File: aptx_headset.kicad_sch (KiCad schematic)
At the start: 63 parts, among them J1 AudioJack4, J2 Conn_01x03, SW1 vol+, SW2 vol-, SW3 next, SW4 prev, SW5 pp/call, SW6 mute, U1 OPA1664, U2 CSR8645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

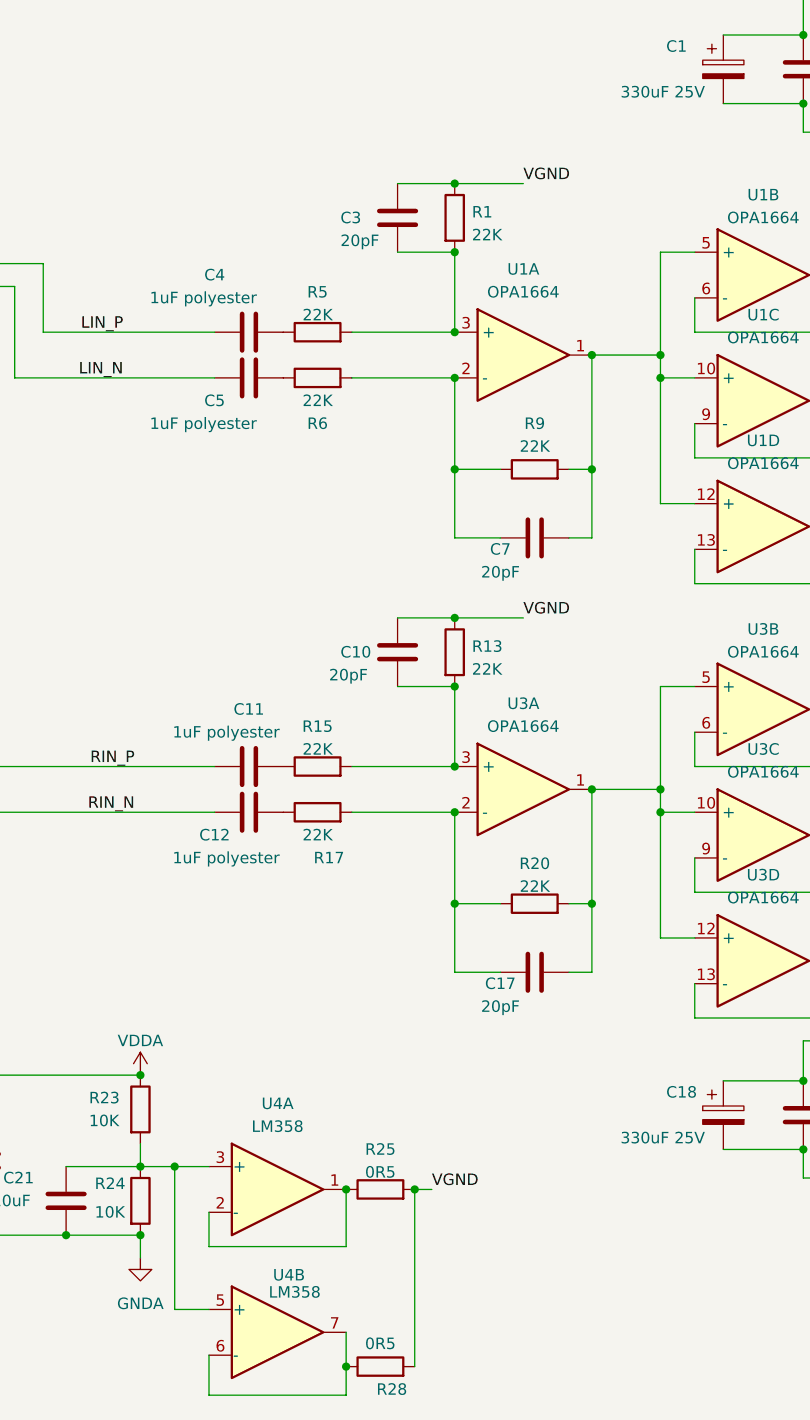
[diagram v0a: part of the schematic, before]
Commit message: separate buffered VGND
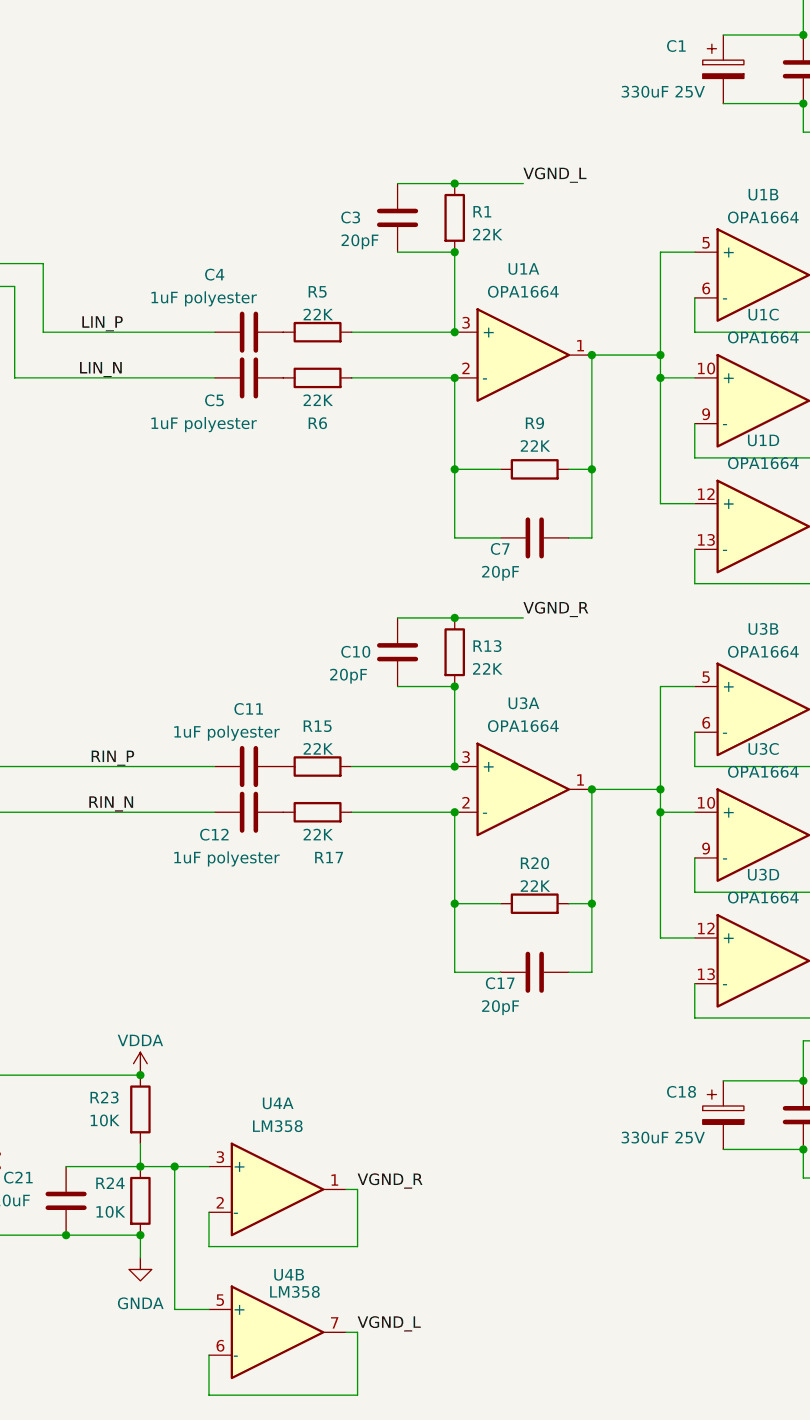
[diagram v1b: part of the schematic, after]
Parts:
- removed R25, R28: 0R5, 00_hari:R_0603_1608Metric_Pad0.98x0.95mm_HandSolder, symbol Device:R
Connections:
- net VGND_R: now reaches U4.1, U4.2 (-)
- net VGND_R: now also C10.1, R13.1
- net VGND_L: now reaches U4.6 (-), U4.7
- net VGND_L: now also C3.1, R1.1
- removed net VGND: C10.1, C3.1, R1.1, R13.1
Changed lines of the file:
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@@
   (junction (at 27.305 57.785) (diameter 0) (color 0 0 0 0)
   )
-  (junction (at 163.83 180.34) (diameter 0) (color 0 0 0 0)
-  )
   (junction (at 73.025 127.635) (diameter 0) (color 0 0 0 0)
   )
@@
   (junction (at 217.805 135.255) (diameter 0) (color 0 0 0 0)
   )
-  (junction (at 171.45 160.655) (diameter 0) (color 0 0 0 0)
-  )
   (junction (at 175.895 97.155) (diameter 0) (color 0 0 0 0)
   )
@@
   )
   (junction (at 132.715 165.735) (diameter 0) (color 0 0 0 0)
-  )
-  (junction (at 163.83 160.655) (diameter 0) (color 0 0 0 0)
   )
   (junction (at 217.805 107.315) (diameter 0) (color 0 0 0 0)
@@
     (stroke (width 0) (type default))
   )
-  (wire (pts (xy 148.59 183.515) (xy 163.83 183.515))
+  (wire (pts (xy 148.59 183.515) (xy 165.1 183.515))
     (stroke (width 0) (type default))
   )
@@
     (stroke (width 0) (type default))
   )
-  (wire (pts (xy 148.59 167.005) (xy 163.83 167.005))
+  (wire (pts (xy 148.59 167.005) (xy 165.1 167.005))
     (stroke (width 0) (type default))
   )
@@
     (stroke (width 0) (type default))
   )
-  (wire (pts (xy 163.83 176.53) (xy 163.83 180.34))
-    (stroke (width 0) (type default))
-  )
   (wire (pts (xy 202.565 61.595) (xy 202.565 65.405))
     (stroke (width 0) (type default))
@@
     (stroke (width 0) (type default))
   )
-  (wire (pts (xy 171.45 160.655) (xy 171.45 180.34))
-    (stroke (width 0) (type default))
-  )
   (wire (pts (xy 132.715 165.735) (xy 140.97 165.735))
     (stroke (width 0) (type default))
@@
     (stroke (width 0) (type default))
   )
-  (wire (pts (xy 163.83 160.655) (xy 163.83 167.005))
+  (wire (pts (xy 165.1 160.655) (xy 165.1 167.005))
     (stroke (width 0) (type default))
   )
@@
     (stroke (width 0) (type default))
   )
-  (wire (pts (xy 173.355 160.655) (xy 171.45 160.655))
-    (stroke (width 0) (type default))
-  )
   (wire (pts (xy 175.895 97.155) (xy 183.515 97.155))
     (stroke (width 0) (type default))
@@
     (stroke (width 0) (type default))
   )
+  (wire (pts (xy 165.1 160.655) (xy 163.83 160.655))
+    (stroke (width 0) (type default))
+  )
   (wire (pts (xy 175.895 118.745) (xy 175.895 128.905))
     (stroke (width 0) (type default))
@@
     (stroke (width 0) (type default))
   )
-  (wire (pts (xy 163.83 180.34) (xy 163.83 183.515))
+  (wire (pts (xy 165.1 176.53) (xy 165.1 183.515))
     (stroke (width 0) (type default))
   )
@@
   )
   (wire (pts (xy 202.565 141.605) (xy 217.805 141.605))
+    (stroke (width 0) (type default))
+  )
+  (wire (pts (xy 165.1 176.53) (xy 163.83 176.53))
     (stroke (width 0) (type default))
   )
@@
     (effects (font (size 1.27 1.27)) (justify left bottom))
   )
-  (label "VGND" (at 173.355 160.655 0) (fields_autoplaced)
+  (label "VGND_R" (at 165.1 160.655 0) (fields_autoplaced)
     (effects (font (size 1.27 1.27)) (justify left bottom))
   )
@@
     (effects (font (size 1.27 1.27)) (justify right bottom))
   )
-  (label "VGND" (at 183.515 48.895 0) (fields_autoplaced)
+  (label "VGND_L" (at 183.515 48.895 0) (fields_autoplaced)
     (effects (font (size 1.27 1.27)) (justify left bottom))
   )
@@
     (effects (font (size 1.27 1.27)) (justify left bottom))
   )
+  (label "VGND_L" (at 165.1 176.53 0) (fields_autoplaced)
+    (effects (font (size 1.27 1.27)) (justify left bottom))
+  )
   (label "MUTE" (at 43.18 169.545 0) (fields_autoplaced)
     (effects (font (size 1.27 1.27)) (justify left bottom))
@@
     (effects (font (size 1.27 1.27)) (justify left bottom))
   )
-  (label "VGND" (at 183.515 97.155 0) (fields_autoplaced)
+  (label "VGND_R" (at 183.515 97.155 0) (fields_autoplaced)
     (effects (font (size 1.27 1.27)) (justify left bottom))
   )
@@
     )
     (property "Datasheet" "~" (id 3) (at 224.155 86.995 0)
-      (effects (font (size 1.27 1.27)) hide)
-    )
-    (pin "1")
-    (pin "2")
-  )
-  (symbol (lib_id "Device:R") (at 167.64 160.655 90) (unit 1)
-    (in_bom yes) (on_board yes) (fields_autoplaced)
-    (property "Reference" "R25" (id 0) (at 167.64 156.21 90)
-      (effects (font (size 1.27 1.27)))
-    )
-    (property "Value" "0R5" (id 1) (at 167.64 158.75 90)
-      (effects (font (size 1.27 1.27)))
-    )
-    (property "Footprint" "00_hari:R_0603_1608Metric_Pad0.98x0.95mm_HandSolder" (id 2) (at 167.64 162.433 90)
-      (effects (font (size 1.27 1.27)) hide)
-    )
-    (property "Datasheet" "~" (id 3) (at 167.64 160.655 0)
       (effects (font (size 1.27 1.27)) hide)
     )
@@
     (pin "2")
   )
-  (symbol (lib_id "Device:R") (at 167.64 180.34 90) (unit 1)
-    (in_bom yes) (on_board yes)
-    (property "Reference" "R28" (id 0) (at 168.91 182.88 90)
-      (effects (font (size 1.27 1.27)))
-    )
-    (property "Value" "0R5" (id 1) (at 167.64 177.8 90)
-      (effects (font (size 1.27 1.27)))
-    )
-    (property "Footprint" "00_hari:R_0603_1608Metric_Pad0.98x0.95mm_HandSolder" (id 2) (at 167.64 182.118 90)
-      (effects (font (size 1.27 1.27)) hide)
-    )
-    (property "Datasheet" "~" (id 3) (at 167.64 180.34 0)
-      (effects (font (size 1.27 1.27)) hide)
-    )
-    (pin "1")
-    (pin "2")
-  )
   (symbol (lib_id "power:GNDA") (at 80.01 177.8 0) (unit 1)
     (in_bom yes) (on_board yes) (fields_autoplaced)
@@
       (reference "R24") (unit 1) (value "10K") (footprint "00_hari:R_0603_1608Metric_Pad0.98x0.95mm_HandSolder")
     )
-    (path "/25c6ea34-99c1-4255-b7f7-b2b1fe148aa9"
-      (reference "R25") (unit 1) (value "0R5") (footprint "00_hari:R_0603_1608Metric_Pad0.98x0.95mm_HandSolder")
-    )
-    (path "/a18a5ff0-8934-4b72-be34-76c1649d5477"
-      (reference "R28") (unit 1) (value "0R5") (footprint "00_hari:R_0603_1608Metric_Pad0.98x0.95mm_HandSolder")
-    )
     (path "/420b7100-3339-4c65-81a9-29cfe6e9151b"
